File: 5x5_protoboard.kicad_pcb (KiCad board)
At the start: 2 copper layers, 50 x 50 mm, 93 parts, among them CON1 BARREL_JACK, CON2 USB-MINI-B, CON3 USB-MICRO, J1 PINS_3X1, J10 PINS_3X1, J11 PINS_3X1, J12 PINS_3X1, J13 PINS_3X1, J14 PINS_3X1, J15 PINS_3X1, J16 PINS_3X1, J17 PINS_3X1, J18 PINS_3X1, J19 PINS_3X1, J2 PINS_3X1, J20 PINS_3X1, J21 PINS_3X1, J22 PINS_3X1, J23 PINS_3X1, J24 PINS_3X1, J25 PINS_3X1, J26 PINS_3X1, J27 PINS_3X1, J28 PINS_3X1, J29 PINS_3X1, J3 PINS_3X1, J30 PINS_3X1, J31 PINS_3X1, J32 PINS_3X1, J33 PINS_3X1, J34 PINS_3X1, J35 PINS_3X1, J36 PINS_3X1, J37 PINS_3X1, J38 PINS_3X1, J39 PINS_3X1, J4 PINS_3X1, J40 PINS_3X1, J41 PINS_3X1, J42 PINS_3X1, J43 PINS_3X1, J44 PINS_3X1, J45 PINS_3X1, J46 PINS_3X1, J47 PINS_3X1, J48 PINS_3X1, J49 PINS_3X1, J5 PINS_3X1, J50 PINS_3X1, J51 PINS_3X1, J52 PINS_3X1, J53 PINS_3X1, J54 PINS_3X1, J55 PINS_3X1, J56 PINS_3X1, J57 PINS_3X1, J58 PINS_3X1, J59 PINS_3X1, J6 PINS_3X1, J60 PINS_3X1, J61 PINS_3X1, J62 PINS_3X1, J63 PINS_3X1, J64 PINS_3X1, J65 PINS_2X1, J7 PINS_3X1, J8 PINS_3X1, J9 PINS_3X1, P1 CONN_5, U1 7805

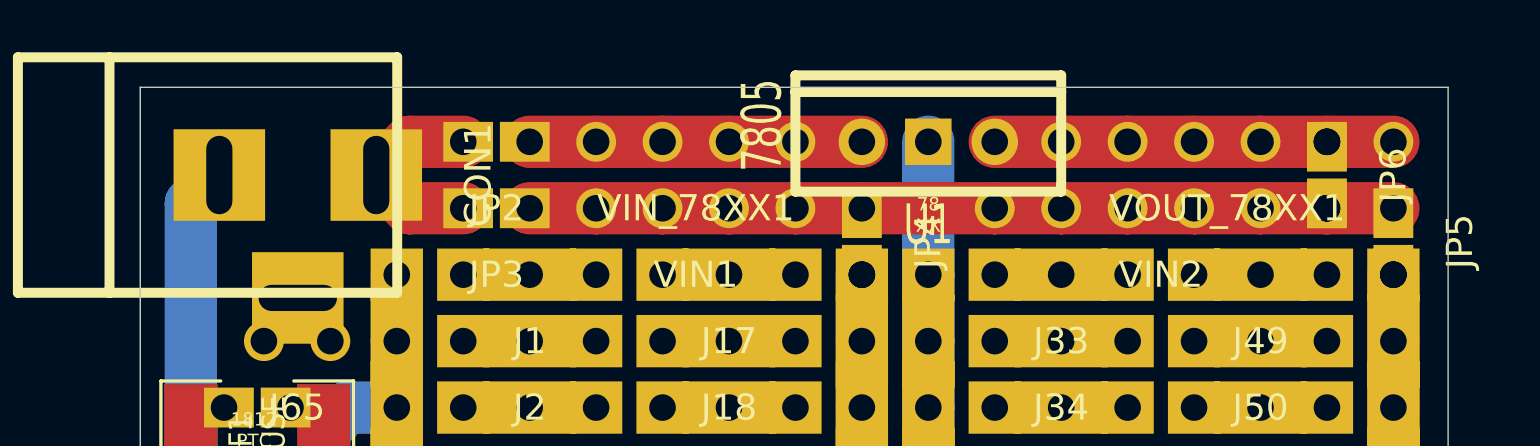
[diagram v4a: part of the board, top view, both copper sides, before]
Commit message: created silk screen markings for power rails
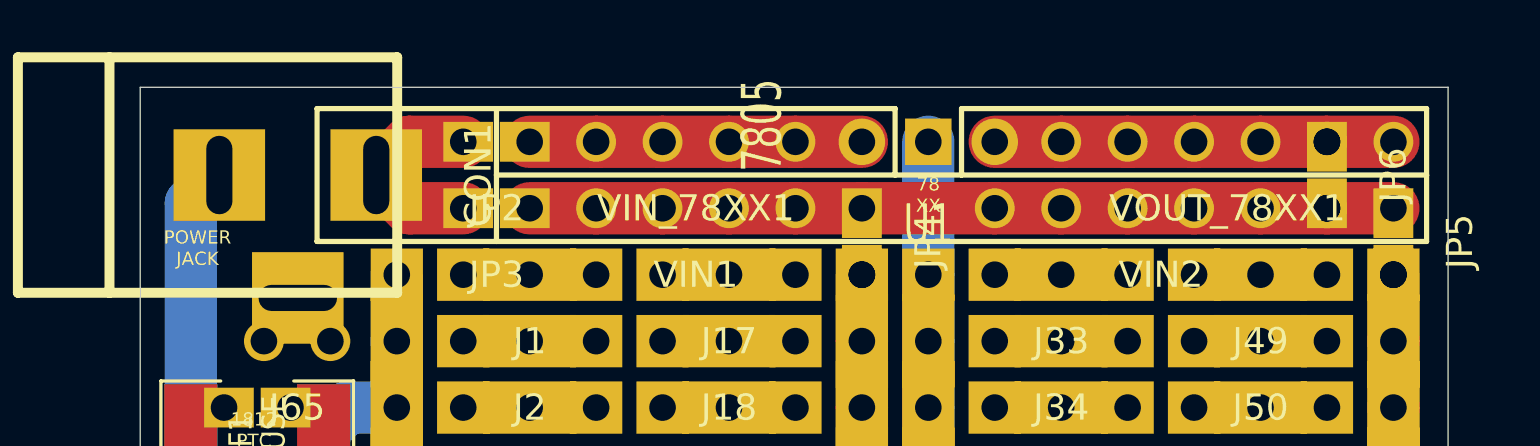
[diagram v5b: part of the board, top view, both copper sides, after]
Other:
- board text added: "POWER JACK"
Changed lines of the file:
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@@
     (links 253)
     (no_connects 132)
-    (area 29.549299 22.033299 79.574701 72.058701)
+    (area 22.31355 18.53692 80.839 73.219)
     (thickness 1.6)
-    (drawings 19)
+    (drawings 49)
     (tracks 137)
     (zones 0)
@@
     (add_net N-0000086)
   )
+  (module 7805_VERT (layer F.Cu)
+    (at 59.69 24.13 90)
+    (descr "Regulateur TO220 serie LM78xx")
+    (tags "TR TO220")
+    (fp_text reference U1 (at -3.175 0 180) (layer F.SilkS)
+      (effects (font (size 1.524 1.016) (thickness 0.2032)))
+    )
+    (fp_text value 7805 (at 0.635 -6.35 90) (layer F.SilkS)
+      (effects (font (size 1.524 1.016) (thickness 0.2032)))
+    )
+    (pad VI thru_hole circle (at 0 -2.54 90) (size 1.778 1.778) (drill 1.016)
+      (layers *.Cu *.Mask F.SilkS)
+      (net 52 N-0000060)
+    )
+    (pad GND thru_hole rect (at 0 0 90) (size 1.778 1.778) (drill 1.016)
+      (layers *.Cu *.Mask F.SilkS)
+      (net 75 N-0000083)
+    )
+    (pad VO thru_hole circle (at 0 2.54 90) (size 1.778 1.778) (drill 1.016)
+      (layers *.Cu *.Mask F.SilkS)
+      (net 49 N-0000058)
+    )
+  )
   (module PINS_6X1 (layer F.Cu)
     (at 71.12 24.13)
@@
     )
   )
-  (module 7805_VERT (layer F.Cu)
-    (at 59.69 24.13 90)
-    (descr "Regulateur TO220 serie LM78xx")
-    (tags "TR TO220")
-    (fp_text reference U1 (at -3.175 0 180) (layer F.SilkS)
-      (effects (font (size 1.524 1.016) (thickness 0.2032)))
-    )
-    (fp_text value 7805 (at 0.635 -6.35 90) (layer F.SilkS)
-      (effects (font (size 1.524 1.016) (thickness 0.2032)))
-    )
-    (fp_line (start 1.905 -5.08) (end 2.54 -5.08) (layer F.SilkS) (width 0.381))
-    (fp_line (start 2.54 -5.08) (end 2.54 5.08) (layer F.SilkS) (width 0.381))
-    (fp_line (start 2.54 5.08) (end 1.905 5.08) (layer F.SilkS) (width 0.381))
-    (fp_line (start -1.905 -5.08) (end 1.905 -5.08) (layer F.SilkS) (width 0.381))
-    (fp_line (start 1.905 -5.08) (end 1.905 5.08) (layer F.SilkS) (width 0.381))
-    (fp_line (start 1.905 5.08) (end -1.905 5.08) (layer F.SilkS) (width 0.381))
-    (fp_line (start -1.905 5.08) (end -1.905 -5.08) (layer F.SilkS) (width 0.381))
-    (pad VI thru_hole circle (at 0 -2.54 90) (size 1.778 1.778) (drill 1.016)
-      (layers *.Cu *.Mask F.SilkS)
-      (net 52 N-0000060)
-    )
-    (pad GND thru_hole rect (at 0 0 90) (size 1.778 1.778) (drill 1.016)
-      (layers *.Cu *.Mask F.SilkS)
-      (net 75 N-0000083)
-    )
-    (pad VO thru_hole circle (at 0 2.54 90) (size 1.778 1.778) (drill 1.016)
-      (layers *.Cu *.Mask F.SilkS)
-      (net 49 N-0000058)
-    )
-  )
   (module PINS_5X1 (layer F.Cu)
     (at 36.83 44.45 270)
@@
     )
   )
+  (gr_text "POWER\nJACK" (at 31.75 28.194) (layer F.SilkS)
+    (effects (font (size 0.508 0.508) (thickness 0.127)))
+  )
+  (gr_line (start 36.322 27.94) (end 43.18 27.94) (angle 90) (layer F.SilkS) (width 0.2))
+  (gr_line (start 36.322 22.86) (end 36.322 27.94) (angle 90) (layer F.SilkS) (width 0.2))
+  (gr_line (start 43.18 22.86) (end 36.322 22.86) (angle 90) (layer F.SilkS) (width 0.2))
+  (gr_line (start 36.322 22.86) (end 43.18 22.86) (angle 90) (layer B.SilkS) (width 0.2))
+  (gr_line (start 36.322 27.94) (end 36.322 22.86) (angle 90) (layer B.SilkS) (width 0.2))
+  (gr_line (start 43.18 27.94) (end 36.322 27.94) (angle 90) (layer B.SilkS) (width 0.2))
+  (gr_line (start 43.18 27.94) (end 43.18 25.4) (angle 90) (layer B.SilkS) (width 0.2))
+  (gr_line (start 78.74 27.94) (end 43.18 27.94) (angle 90) (layer B.SilkS) (width 0.2))
+  (gr_line (start 78.74 25.4) (end 78.74 27.94) (angle 90) (layer B.SilkS) (width 0.2))
+  (gr_line (start 43.18 25.4) (end 58.42 25.4) (angle 90) (layer B.SilkS) (width 0.2))
+  (gr_line (start 43.18 22.86) (end 43.18 25.4) (angle 90) (layer B.SilkS) (width 0.2))
+  (gr_line (start 58.42 22.86) (end 43.18 22.86) (angle 90) (layer B.SilkS) (width 0.2))
+  (gr_line (start 58.42 25.4) (end 58.42 22.86) (angle 90) (layer B.SilkS) (width 0.2))
+  (gr_line (start 60.96 25.4) (end 58.42 25.4) (angle 90) (layer B.SilkS) (width 0.2))
+  (gr_line (start 78.74 25.4) (end 60.96 25.4) (angle 90) (layer B.SilkS) (width 0.2))
+  (gr_line (start 78.74 22.86) (end 78.74 25.4) (angle 90) (layer B.SilkS) (width 0.2))
+  (gr_line (start 60.96 22.86) (end 78.74 22.86) (angle 90) (layer B.SilkS) (width 0.2))
+  (gr_line (start 60.96 25.146) (end 60.96 22.86) (angle 90) (layer B.SilkS) (width 0.2))
+  (gr_line (start 78.74 22.86) (end 78.74 25.4) (angle 90) (layer F.SilkS) (width 0.2))
+  (gr_line (start 60.96 22.86) (end 78.74 22.86) (angle 90) (layer F.SilkS) (width 0.2))
+  (gr_line (start 60.96 25.4) (end 60.96 22.86) (angle 90) (layer F.SilkS) (width 0.2))
+  (gr_line (start 43.18 22.86) (end 43.18 25.4) (angle 90) (layer F.SilkS) (width 0.2))
+  (gr_line (start 58.42 22.86) (end 43.18 22.86) (angle 90) (layer F.SilkS) (width 0.2))
+  (gr_line (start 58.42 25.4) (end 58.42 22.86) (angle 90) (layer F.SilkS) (width 0.2))
+  (gr_line (start 43.18 25.4) (end 60.96 25.4) (angle 90) (layer F.SilkS) (width 0.2))
+  (gr_line (start 43.18 27.94) (end 43.18 25.4) (angle 90) (layer F.SilkS) (width 0.2))
+  (gr_line (start 78.74 27.94) (end 43.18 27.94) (angle 90) (layer F.SilkS) (width 0.2))
+  (gr_line (start 78.74 25.4) (end 78.74 27.94) (angle 90) (layer F.SilkS) (width 0.2))
+  (gr_line (start 78.74 25.4) (end 60.96 25.4) (angle 90) (layer F.SilkS) (width 0.2))
   (gr_text GND (at 36.068 38.1 90) (layer F.SilkS)
     (effects (font (size 0.508 0.508) (thickness 0.127)))
@@
     (effects (font (size 0.508 0.508) (thickness 0.127)))
   )
-  (gr_text "78\nXX" (at 59.69 26.924) (layer F.SilkS)
+  (gr_text "78\nXX" (at 59.69 26.162) (layer F.SilkS)
     (effects (font (size 0.508 0.508) (thickness 0.127)))
   )

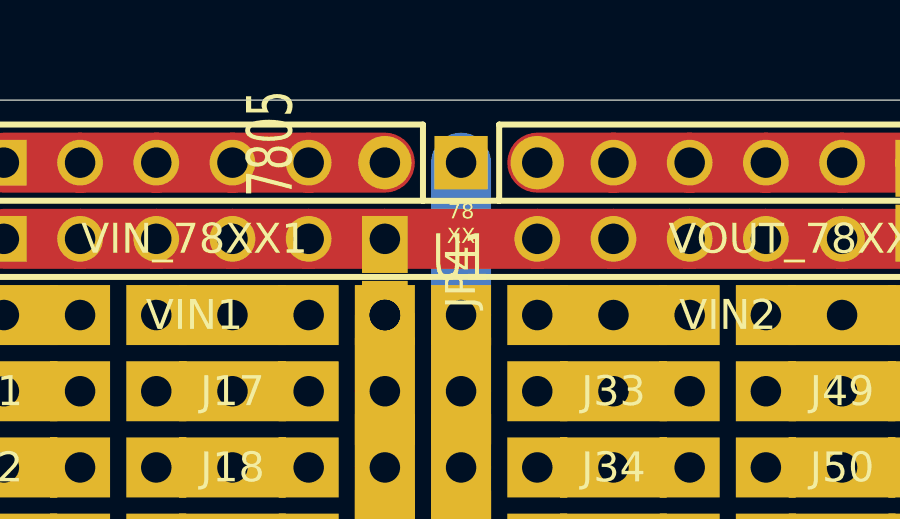
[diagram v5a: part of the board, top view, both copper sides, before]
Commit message: added 0603 suppersion caps to 78xx regulator
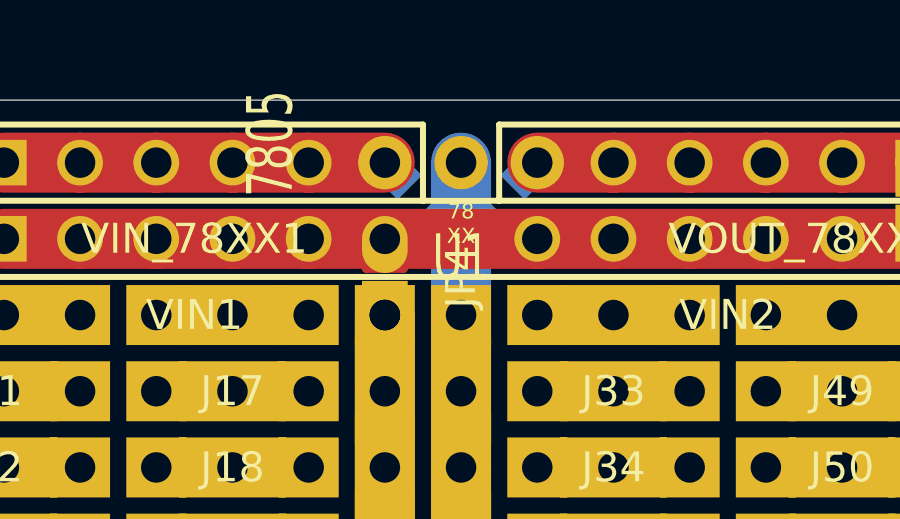
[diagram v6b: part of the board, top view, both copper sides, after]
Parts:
- added C1: u33, SM0603_Capa, B.Cu at (58.3, 25.3)
- added C2: u1, SM0603_Capa, B.Cu at (61.1, 25.3)
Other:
- board text added: "100n"
- board text added: "330n"

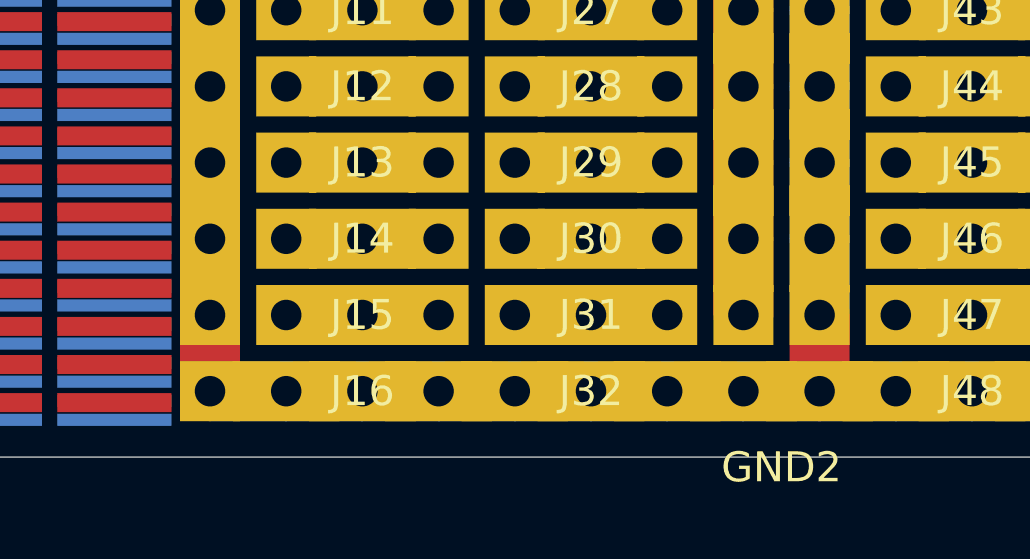
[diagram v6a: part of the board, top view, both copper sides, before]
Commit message: fixed bug where gnd rails where only connected on the front of the pcb
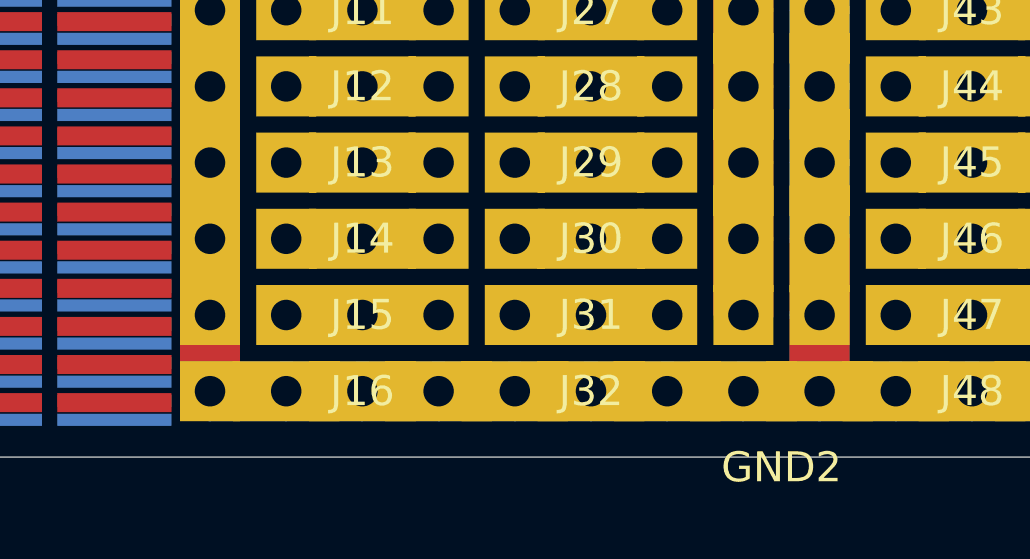
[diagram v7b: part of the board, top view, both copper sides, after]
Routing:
- net N-0000083: track 127.6 -> 137.8 mm
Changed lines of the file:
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@@
     (thickness 1.6)
     (drawings 50)
-    (tracks 137)
+    (tracks 139)
     (zones 0)
     (modules 95)
@@
   (page A3)
   (layers
-    (15 F.Cu signal)
+    (15 F.Cu signal hide)
     (0 B.Cu signal)
     (16 B.Adhes user)
@@
     (20 B.SilkS user)
     (21 F.SilkS user)
-    (22 B.Mask user)
-    (23 F.Mask user)
+    (22 B.Mask user hide)
+    (23 F.Mask user hide)
     (24 Dwgs.User user)
     (25 Cmts.User user)
@@
   (segment (start 72.39 26.67) (end 74.93 26.67) (width 2) (layer F.Cu) (net 51))
   (segment (start 74.93 26.67) (end 77.47 26.67) (width 2) (layer F.Cu) (net 51))
-  (segment (start 39.37 69.85) (end 39.37 67.31) (width 2) (layer F.Cu) (net 75))
-  (segment (start 59.69 69.85) (end 59.69 67.31) (width 2) (layer F.Cu) (net 75))
+  (segment (start 39.37 69.85) (end 39.37 64.77) (width 2) (layer F.Cu) (net 75) (status C00000))
+  (segment (start 59.69 64.77) (end 59.69 69.85) (width 2) (layer F.Cu) (net 75) (status C00000))
+  (segment (start 39.37 69.85) (end 39.37 67.31) (width 2) (layer B.Cu) (net 75))
+  (segment (start 59.69 67.31) (end 59.69 69.85) (width 2) (layer B.Cu) (net 75))
   (segment (start 39.37 34.29) (end 37.465 34.29) (width 2) (layer B.Cu) (net 75))
   (segment (start 37.465 34.29) (end 36.576 35.179) (width 2) (layer B.Cu) (net 75))
